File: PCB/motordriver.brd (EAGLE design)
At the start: 100 x 80 mm, 46 parts, among them IC1 7818TV

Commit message: PCB/motordriver.sch
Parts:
- removed OUT, OUT1, OUT2, OUT3: SMDPAD, myLibrary:1.5X7MMPAD
- added C10: (no value), rcl:C0805K
- added OUT1_JMP_A, OUT1_JMP_B, OUT2_JMP_A, OUT2_JMP_B: SMDPAD, myLibrary:1.5X7MMPAD
- added R11: 10k, myLibrary:0805
- added R12: 10k, myLibrary:3X1MM
- added R13: 160, myLibrary:0805
- added VD1, VD2: 3.3V, zener:DO35-7
- moved C9 0.81 mm to (51.1, 39.0)
- renumbered 100K1 to R14
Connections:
- removed net N$12: OUT1.P$1, OUT3.P$1, U$2.14, U$2.15
- removed net N$13: OUT.P$1, OUT2.P$1, U$2.18, U$2.19
- removed net TOARM: R8.2, U$2.2
- new net B: IN1.P$1, IN3.P$1, R13.P$1, R2.P$1
- new net OUT1: OUT1_JMP_A.P$1, OUT1_JMP_B.P$1, U$2.18, U$2.19
- new net OUT2: OUT2_JMP_A.P$1, OUT2_JMP_B.P$1, U$2.14, U$2.15
- new net PA10: U$1.P$7
- new net PA11: U$1.P$8
- new net PA12: U$1.P$9
- new net PA2: R6.P$2, U$1.P$34, U$2.12, VD2.C
- new net PA3: C7.1, R13.P$2, U$1.P$33
- new net PA4: U$1.P$32
- new net PA5: U$1.P$31
- new net PA6: U$1.P$30
- new net PA7: U$1.P$29
- new net PA8: U$1.P$5
- new net PA9: U$1.P$6
- new net PB1: R8.2, U$1.P$27, U$2.2
- new net PB10: U$1.P$26
- new net PB15: U$1.P$4, U$2.9
- new net PB5: U$1.P$13
- new net PB6: U$1.P$14
- new net PB7: U$1.P$15
- new net PC13: U$1.P$39
- new net PC14: U$1.P$38
- new net PC15: U$1.P$37
- net 3.3V: now also R11.P$1
- net GND: now also C10.2, R12.-, VD1.A, VD2.A
- net N$26: now also C10.1
- net PA0: no longer R6.P$2, U$2.12
- net PA1: now also VD1.C
- net PA15: no longer C7.1, IN1.P$1, IN3.P$1, R2.P$1
- net PB0: now also R11.P$2, R12.+, R12.FLOATING
- net PB4: no longer U$2.9
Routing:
- net 3.3V: track 97.6 -> 200.4 mm, vias 2 -> 4
- net PB0: track 0.00 -> 94.6 mm
- net PA2: track 0.00 -> 88.3 mm, vias 0 -> 1
- net PB15: track 0.00 -> 83.5 mm, vias 0 -> 2
- net PB1: track 0.00 -> 83.5 mm, vias 0 -> 3
- net PB4: track 65.0 -> 0.00 mm, vias 1 -> 0
- net PA0: track 60.1 -> 0.00 mm, vias 1 -> 0
- net OUT2: track 0.00 -> 49.8 mm, vias 0 -> 3
- net N$12: track 49.8 -> 0.00 mm, vias 3 -> 0
- net PA3: track 0.00 -> 49.8 mm, vias 0 -> 1
- net PA15: track 46.5 -> 0.00 mm, vias 2 -> 0
- net OUT1: track 0.00 -> 44.8 mm, vias 0 -> 3
- net N$13: track 44.8 -> 0.00 mm, vias 3 -> 0
- net B: track 0.00 -> 23.0 mm, vias 0 -> 1
- net GND: track 248.6 -> 227.7 mm, vias 25 -> 24
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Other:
- board size 100 x 80 mm -> 100.1 x 80.1 mm
- board text added: "3.3V"
- board text added: "C1"
- board text added: "C10"
- board text added: "C2"
- board text added: "C3"
- board text added: "C4"
- board text added: "C5"
- board text added: "C6"
- board text added: "C7"
- board text added: "C8"
- board text added: "C9"
- board text added: "ERROR"
- board text added: "FUSE"
- board text added: "IC1"
- board text added: "LED"
- board text added: "MODE"
- board text added: "Max"
- board text added: "Min"
- board text added: "NOL"
- board text added: "R1"
- board text added: "R10"
- board text added: "R11"
- board text added: "R13"
- board text added: "R14"
- board text added: "R2"
- board text added: "R3"
- board text added: "R4"
- board text added: "R5"
- board text added: "R6"
- board text added: "R7"
- board text added: "R8"
- board text added: "R9"
- board text added: "SPEED"
- board text added: "STATUS"
- board text added: "T1"
- board text added: "T2"
- board text added: "T3"
- board text added: "drv"
- board text added: "nTRIP"

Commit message: some changes in resistor values.
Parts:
- C10: value (none) -> 100nF
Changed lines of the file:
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@@
 </element>
 <element name="R13" library="myLibrary" package="0805" value="160" x="60.45" y="63.6"/>
-<element name="C10" library="rcl" library_urn="urn:adsk.eagle:library:334" package="C0805K" package3d_urn="urn:adsk.eagle:package:23681/2" value="" x="73.1774" y="33.02" rot="R270">
+<element name="C10" library="rcl" library_urn="urn:adsk.eagle:library:334" package="C0805K" package3d_urn="urn:adsk.eagle:package:23681/2" value="100nF" x="73.1774" y="33.02" rot="R270">
 <attribute name="SPICEPREFIX" value="C" x="73.1774" y="33.02" size="1.778" layer="27" rot="R270" display="off"/>
 </element>

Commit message: software is working. Send the sum of Iprop1 and Iprop2 to application software.
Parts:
- R5, R6: value 420 Ohm -> 402 Ohm
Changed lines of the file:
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@@
 <attribute name="SPICEPREFIX" value="C" x="37.55" y="50.65" size="1.778" layer="27" rot="R270" display="off"/>
 </element>
-<element name="R5" library="myLibrary" package="0805" value="420 Ohm" x="39.8" y="43.55" rot="R270"/>
-<element name="R6" library="myLibrary" package="0805" value="420 Ohm" x="40.3" y="40.05" rot="R90"/>
+<element name="R5" library="myLibrary" package="0805" value="402 Ohm" x="39.8" y="43.55" rot="R270"/>
+<element name="R6" library="myLibrary" package="0805" value="402 Ohm" x="40.3" y="40.05" rot="R90"/>
 <element name="JMP1" library="jump-0r-smd" library_urn="urn:adsk.eagle:library:251" package="A0R-JMP" package3d_urn="urn:adsk.eagle:package:15385/1" value="0R-JUMPA" x="35.56" y="57.531"/>
 <element name="JMP2" library="jump-0r-smd" library_urn="urn:adsk.eagle:library:251" package="A0R-JMP" package3d_urn="urn:adsk.eagle:package:15385/1" value="0R-JUMPA" x="30.226" y="57.531"/>

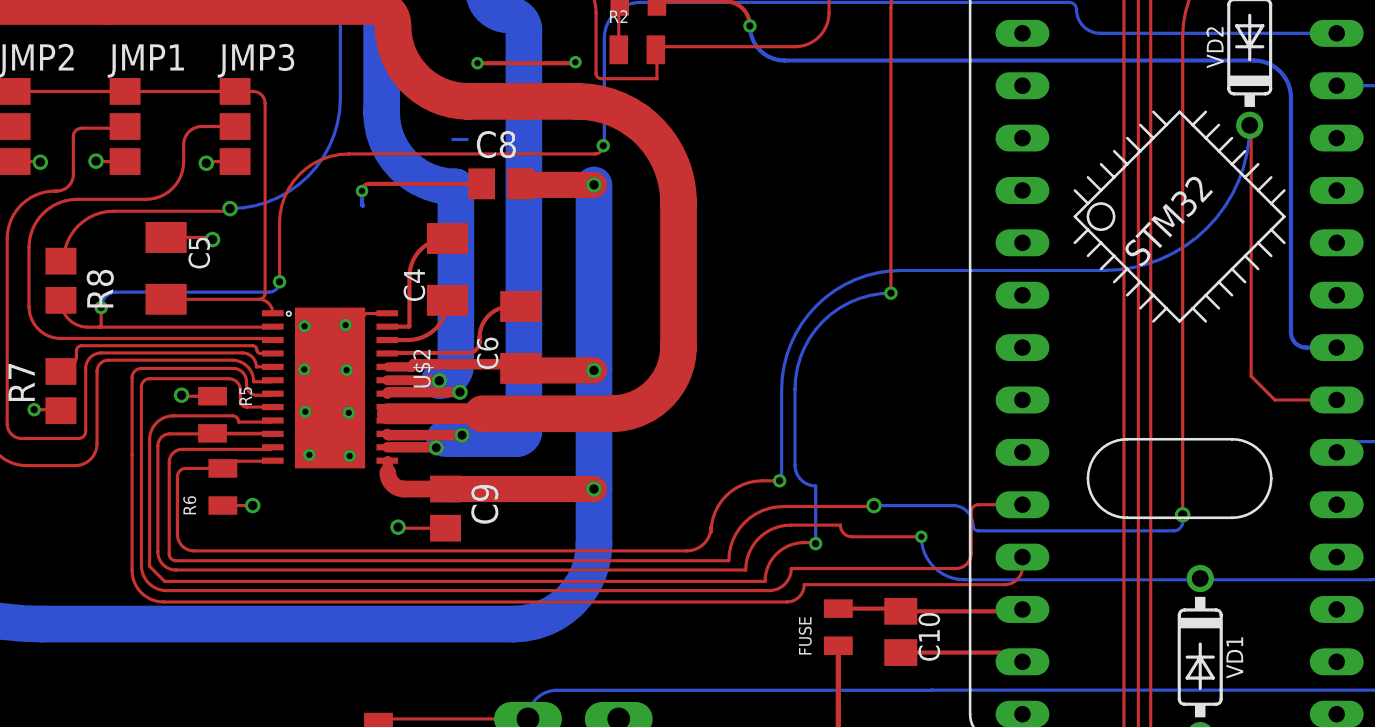
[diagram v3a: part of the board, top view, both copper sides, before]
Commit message: added Low pass rc filter for the IOPROPx output
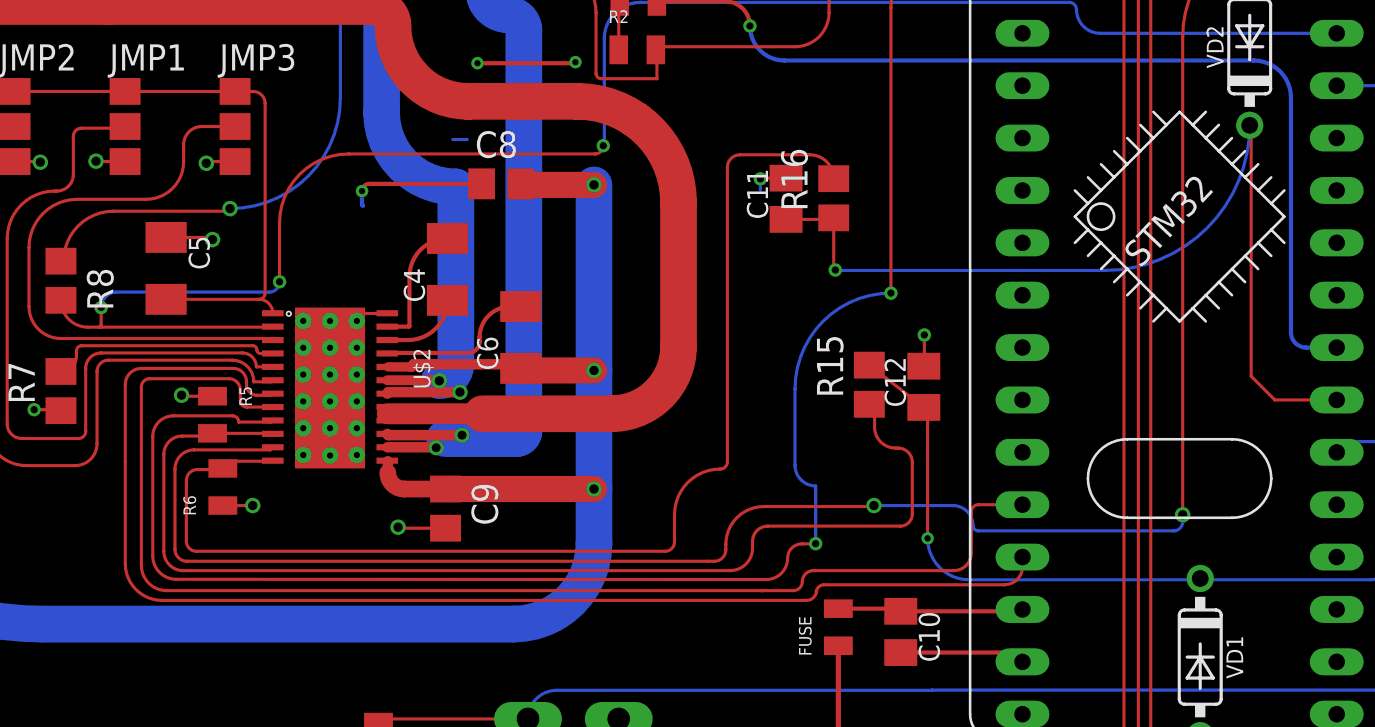
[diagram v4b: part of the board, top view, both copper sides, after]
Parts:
- added C11: (no value), rcl:C0805K
- added C12: 10u, rcl:C0805K
- added R15, R16: 1K, resistor:R0805
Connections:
- new net N$100: R15.1, R5.P$2, U$2.10
- new net N$101: R16.2, R6.P$2, U$2.12
- net GND: now also C11.2, C12.2, U$2.P$1, U$2.P$10, U$2.P$11, U$2.P$12, U$2.P$13, U$2.P$14, U$2.P$15, U$2.P$16, U$2.P$18, U$2.P$19, U$2.P$2, U$2.P$3, U$2.P$4, U$2.P$5, U$2.P$6, U$2.P$7, U$2.P$8, U$2.P$9
- net PA1: now also C12.1, R15.2; no longer R5.P$2, U$2.10
- net PA2: now also C11.1, R16.1; no longer R6.P$2, U$2.12
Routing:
- net N$101: track 0.00 -> 56.7 mm
- net N$100: track 0.00 -> 54.7 mm
- net PA2: track 88.3 -> 44.8 mm
- net PA1: track 84.9 -> 41.9 mm
- net GND: track 227.7 -> 223.5 mm, vias 24 -> 18
- net PB11: track 94.0 -> 93.3 mm
- net PB15: track 83.5 -> 82.9 mm
